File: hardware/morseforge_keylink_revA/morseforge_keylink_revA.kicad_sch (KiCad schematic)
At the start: 18 parts, among them J1 USB_C_Receptacle_USB2.0_14P, J2 Conn_01x02_Socket, SW1 SW_SPST, U1 MCP73831-2-MC, U2 LDO40LPU33RY

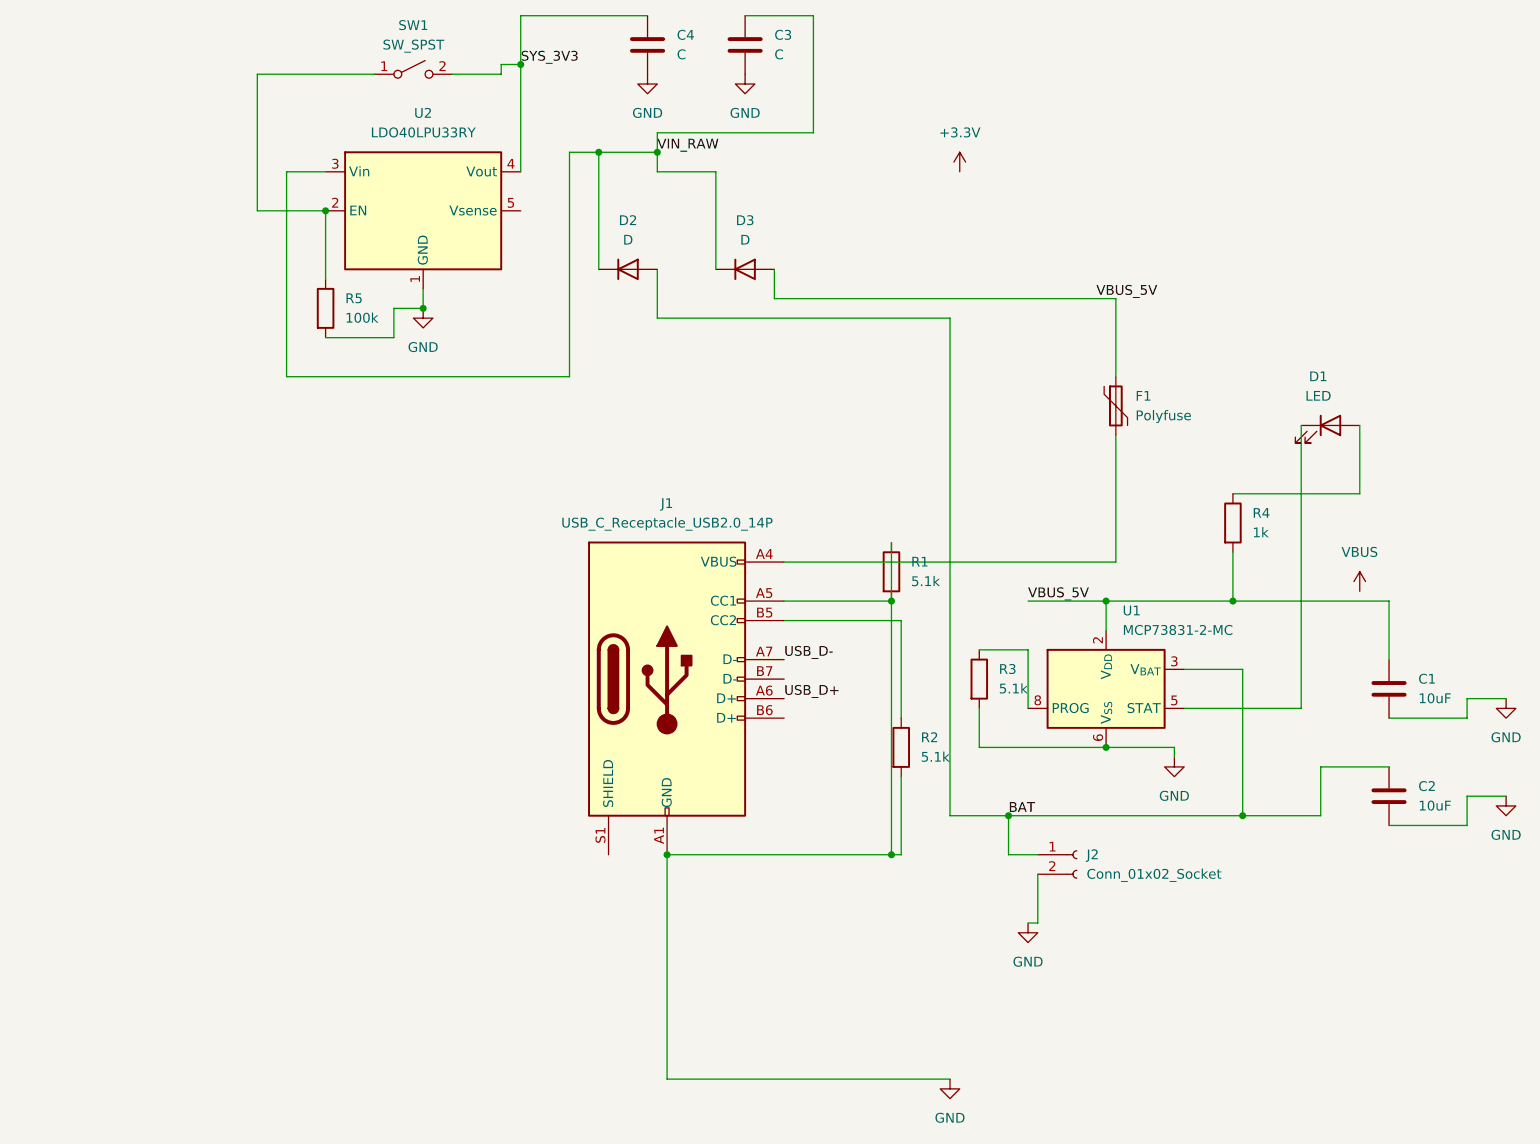
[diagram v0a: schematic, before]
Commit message: Add BLE functionality to firmware and create mobile app
- Updated code.py with BLE UART service for morse key events
- Created Expo React Native mobile app with BLE connectivity
- App connects to ESP32, receives DIT/DAH events, plays audio sidetone
- Configured iOS/Android BLE permissions
- Added tone.wav audio asset
- Includes setup documentation in mobile_app/README.md

Co-Authored-By: Claude Sonnet 4.5 <noreply@anthropic.com>
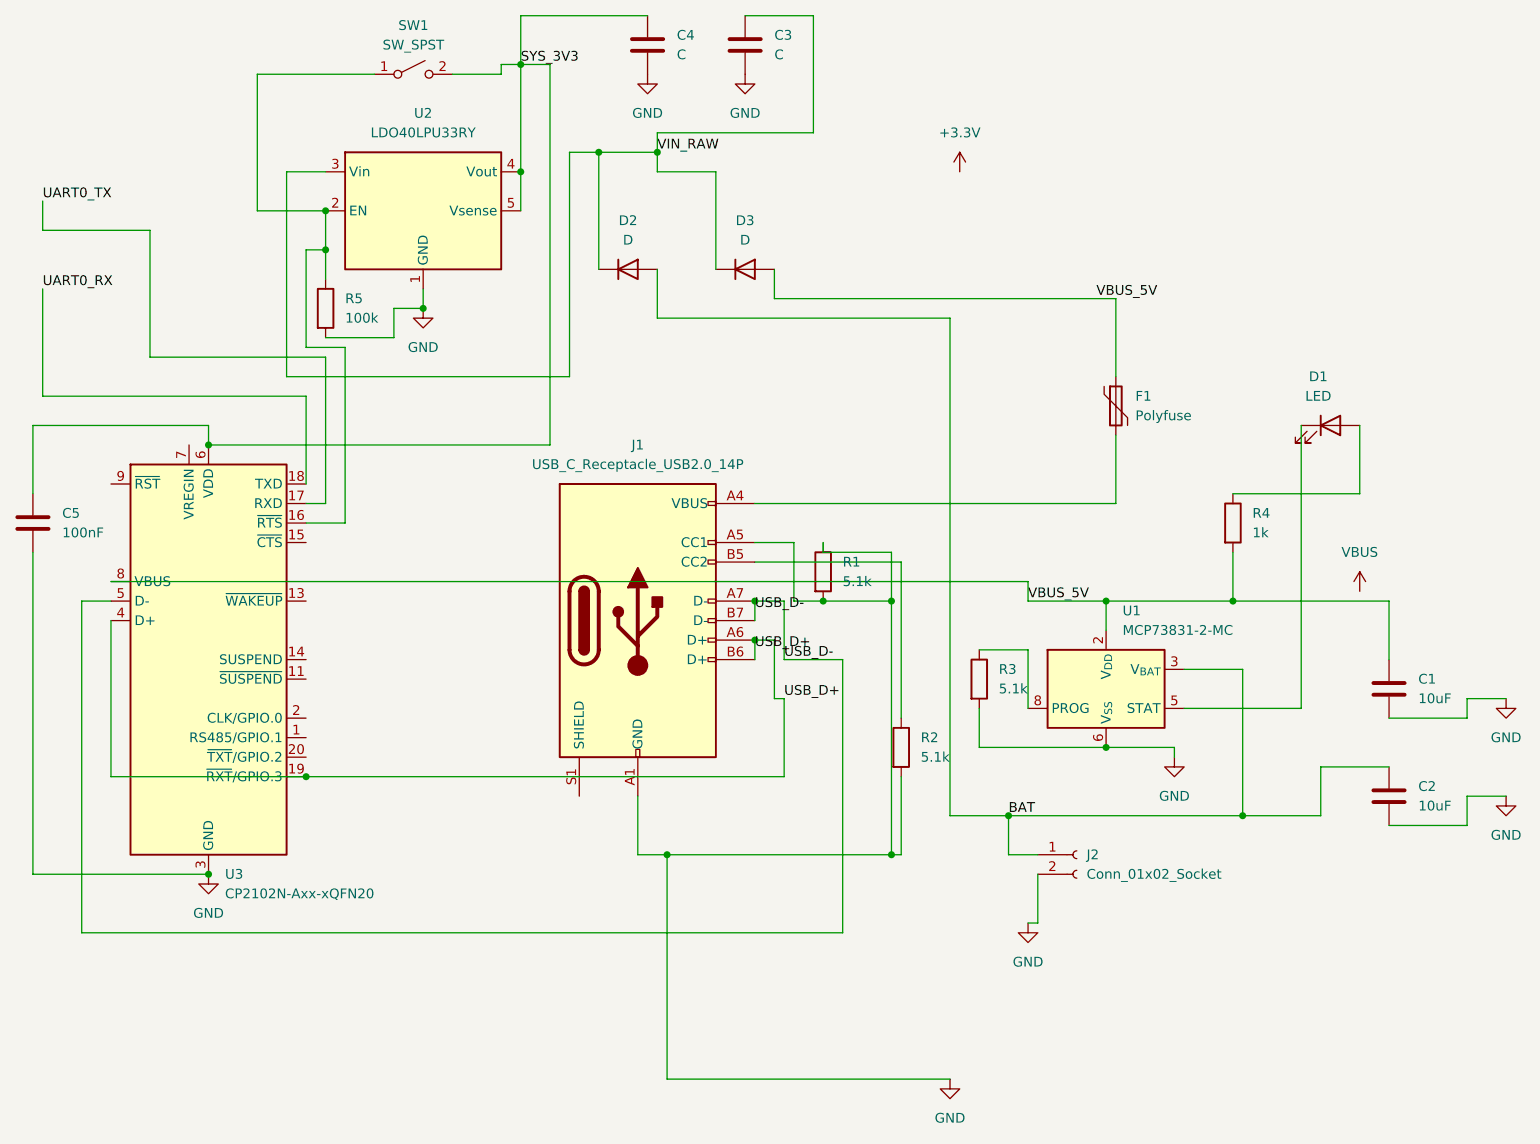
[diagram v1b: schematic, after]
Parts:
- added C5: 100nF, symbol Device:C
- added U3: CP2102N-Axx-xQFN20, Package_DFN_QFN:SiliconLabs_QFN-20-1EP_3x3mm_P0.5mm, symbol Interface_USB:CP2102N-Axx-xQFN20
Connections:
- net GND: now also C5.2, U3.12 (GND), U3.21 (GND), U3.3 (GND)
- net SYS_3V3: now also U2.5 (Vsense), C5.1, U3.6 (VDD)
- net USB_D+: now also J1.B6 (D+), U3.19 (~{RXT}/GPIO.3), U3.4 (D+)
- net USB_D-: now also J1.B7 (D-), U3.5 (D-)
- net VBUS_5V: now also U3.8 (VBUS)
- net at R5.1, SW1.1 (A), U2.2 (EN): now also U3.16 (~{RTS})
- new net UART0_RX: U3.18 (TXD)
- new net UART0_TX: U3.17 (RXD)
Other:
- moved on the sheet: J1, R1
